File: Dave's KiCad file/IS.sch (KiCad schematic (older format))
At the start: 0 parts

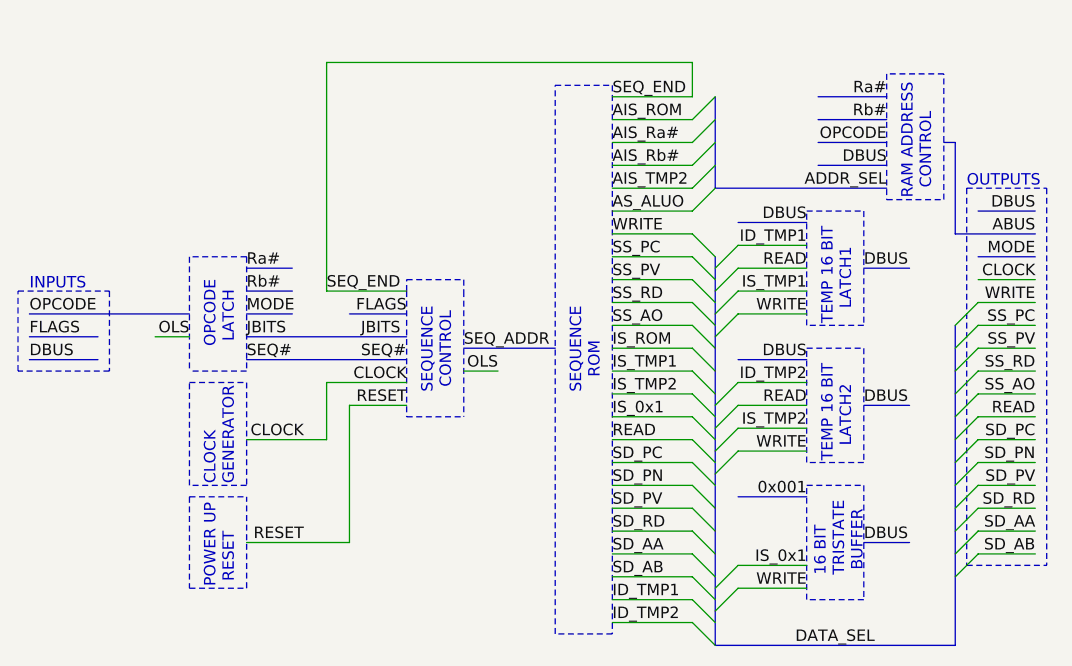
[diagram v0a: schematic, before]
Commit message: Add latch in RAM Address Control
Previously RET and POP Ra relied on using ALU output to put new SP value on RAM address, but that wouldn't work as can't have ALU output on data bus and use data bus for reading from RAM
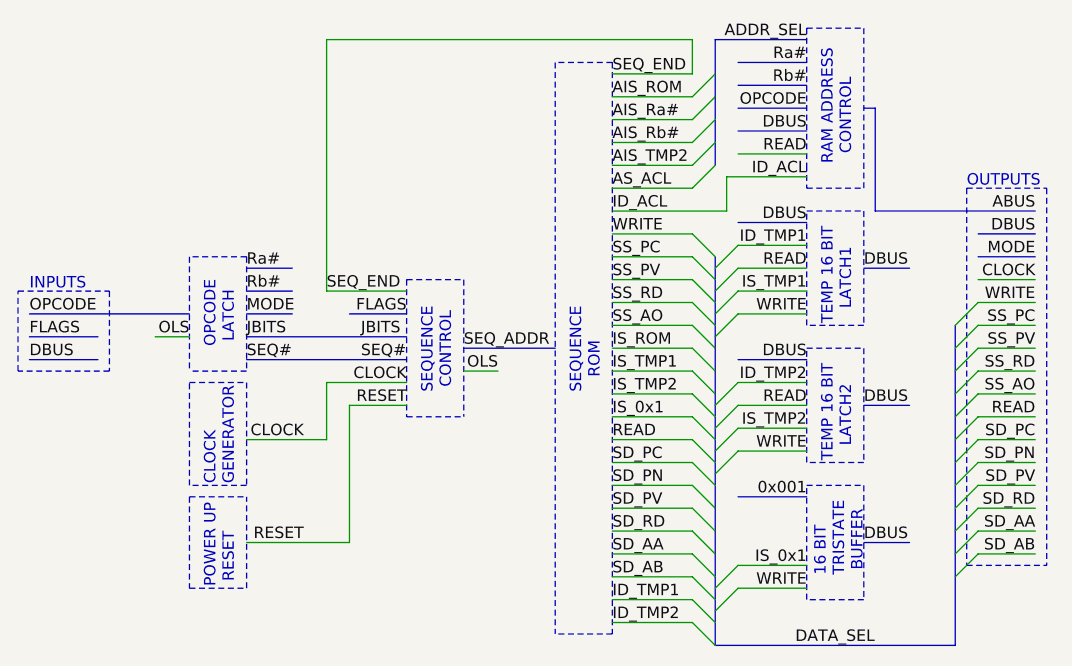
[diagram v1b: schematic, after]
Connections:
- net labels added: AS_ACL, ID_ACL
- net labels removed: AS_ALUO
- wire segments 59 -> 63
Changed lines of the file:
@@
 Text Label 3900 3750 0    50   ~ 0
 IS_0x1
+Text Label 3900 2350 0    50   ~ 0
+AIS_ROM
 Text Label 3900 2450 0    50   ~ 0
-AIS_ROM
+AIS_Ra#
 Text Label 3900 2550 0    50   ~ 0
-AIS_Ra#
+AIS_Rb#
 Text Label 3900 2650 0    50   ~ 0
-AIS_Rb#
+AIS_TMP2
 Text Label 3900 2750 0    50   ~ 0
-AIS_TMP2
-Text Label 3900 2850 0    50   ~ 0
-AS_ALUO
+AS_ACL
 Wire Wire Line
 	2050 3400 1900 3400
@@
 	2300 3550 2050 3550
 Wire Wire Line
+	3900 2650 4250 2650
+Wire Wire Line
+	3900 2550 4250 2550
+Wire Wire Line
+	3900 2450 4250 2450
+Wire Wire Line
+	3900 2350 4250 2350
+Wire Wire Line
 	3900 2750 4250 2750
-Wire Wire Line
-	3900 2650 4250 2650
-Wire Wire Line
-	3900 2550 4250 2550
-Wire Wire Line
-	3900 2450 4250 2450
-Wire Wire Line
-	3900 2850 4250 2850
 Wire Wire Line
 	3900 2950 4250 2950
@@
 	2300 3050 2050 3050
 Wire Wire Line
-	3900 2350 4250 2350
+	3900 2250 4250 2250
 Wire Notes Line style solid rgb(0, 255, 0)
 	2300 3050 2300 3550
 Wire Notes Line style solid rgb(0, 255, 0)
 	2050 3050 2050 3550
-Text Label 3900 2350 0    50   ~ 0
+Text Label 3900 2250 0    50   ~ 0
 SEQ_END
 Wire Notes Line style solid rgb(0, 255, 0)
-	3900 2300 3900 4700
-Wire Notes Line style solid rgb(0, 255, 0)
 	3900 4700 3650 4700
-Wire Notes Line style solid rgb(0, 255, 0)
-	3650 4700 3650 2300
-Wire Notes Line style solid rgb(0, 255, 0)
-	3650 2300 3900 2300
 Text Notes 3200 3650 1    50   ~ 0
 SEQUENCE\n CONTROL
@@
 	2300 3500 3000 3500
 Entry Wire Line
-	4250 2850 4350 2750
-Entry Wire Line
 	4250 2750 4350 2650
 Entry Wire Line
@@
 Entry Wire Line
 	4250 2450 4350 2350
-Text Notes 5300 2800 1    50   ~ 0
+Entry Wire Line
+	4250 2350 4350 2250
+Text Notes 4950 2650 1    50   ~ 0
 RAM ADDRESS\n  CONTROL
-Wire Bus Line
-	4350 2750 5100 2750
-Text Label 5100 2750 2    50   ~ 0
+Text Label 4750 2100 2    50   ~ 0
 ADDR_SEL
-Text Label 5100 2650 2    50   ~ 0
-DBUS
-Text Label 5100 2550 2    50   ~ 0
+Text Label 4750 2500 2    50   ~ 0
+DBUS
+Text Label 4750 2400 2    50   ~ 0
 OPCODE
 Wire Bus Line
-	5100 2550 4800 2550
-Text Label 5100 2350 2    50   ~ 0
+	4750 2400 4450 2400
+Text Label 4750 2200 2    50   ~ 0
 Ra#
-Text Label 5100 2450 2    50   ~ 0
+Text Label 4750 2300 2    50   ~ 0
 Rb#
 Wire Bus Line
-	4800 2650 5100 2650
-Wire Bus Line
-	4800 2450 5100 2450
-Wire Bus Line
-	4800 2350 5100 2350
-Wire Notes Line style solid rgb(0, 255, 0)
-	5100 2250 5100 2800
-Wire Notes Line style solid rgb(0, 255, 0)
-	5100 2800 5350 2800
-Wire Notes Line style solid rgb(0, 255, 0)
-	5350 2800 5350 2250
-Wire Notes Line style solid rgb(0, 255, 0)
-	5350 2250 5100 2250
+	4450 2300 4750 2300
+Wire Bus Line
+	4450 2200 4750 2200
 Wire Wire Line
 	3400 3550 3250 3550
@@
 Wire Bus Line
 	4450 2900 4750 2900
-Wire Notes Line style solid rgb(0, 255, 0)
-	3250 3200 3250 3750
-Wire Notes Line style solid rgb(0, 255, 0)
-	3000 3200 3000 3750
 Wire Bus Line
 	5000 3100 5200 3100
@@
 Wire Notes Line style solid rgb(0, 255, 0)
 	5000 3350 4750 3350
-Wire Bus Line
-	5400 2950 5750 2950
-Wire Bus Line
-	5400 2550 5350 2550
-Wire Bus Line
-	5400 2950 5400 2550
 Wire Notes Line
 	5800 2750 5800 4400
@@
 Wire Notes Line
 	5450 2750 5800 2750
+Text Label 5750 2950 2    50   ~ 0
+DBUS
+Wire Bus Line
+	5500 2950 5750 2950
 Text Label 5750 2850 2    50   ~ 0
-DBUS
-Wire Bus Line
-	5500 2850 5750 2850
-Text Label 5750 2950 2    50   ~ 0
 ABUS
 Entry Wire Line
@@
 	4750 4550 4750 4050
 Wire Wire Line
-	4250 2350 4250 2200
-Wire Wire Line
-	4250 2200 2650 2200
-Wire Wire Line
-	2650 2200 2650 3200
+	4250 2250 4250 2100
+Wire Wire Line
+	4250 2100 2650 2100
 Entry Wire Line
 	4350 4500 4450 4400
@@
 	2650 3200 3000 3200
 Wire Notes Line style solid rgb(0, 255, 0)
-	3000 3200 3000 3150
-Wire Notes Line style solid rgb(0, 255, 0)
 	3000 3150 3250 3150
 Wire Notes Line style solid rgb(0, 255, 0)
-	3250 3150 3250 3200
-Wire Bus Line
-	4350 2350 4350 2750
+	3250 3150 3250 3750
+Wire Notes Line style solid rgb(0, 255, 0)
+	3000 3150 3000 3750
+Text Label 4750 2600 2    50   ~ 0
+READ
+Wire Wire Line
+	4450 2600 4750 2600
+Text Label 3900 2850 0    50   ~ 0
+ID_ACL
+Wire Bus Line
+	4750 2500 4450 2500
+Wire Notes Line style solid rgb(0, 255, 0)
+	4750 2050 5000 2050
+Wire Notes Line style solid rgb(0, 255, 0)
+	4750 2050 4750 2650
+Wire Notes Line style solid rgb(0, 255, 0)
+	5000 2050 5000 2650
+Wire Bus Line
+	4350 2100 4750 2100
+Wire Bus Line
+	5050 2850 5750 2850
+Wire Wire Line
+	2650 2100 2650 3200
+Wire Notes Line style solid rgb(0, 255, 0)
+	3900 2200 3650 2200
+Wire Notes Line style solid rgb(0, 255, 0)
+	3900 2200 3900 4700
+Wire Notes Line style solid rgb(0, 255, 0)
+	3650 2200 3650 4700
+Wire Wire Line
+	3900 2850 4400 2850
+Wire Wire Line
+	4400 2700 4400 2850
+Wire Wire Line
+	4400 2700 4750 2700
+Text Label 4750 2700 2    50   ~ 0
+ID_ACL
+Wire Notes Line style solid rgb(0, 255, 0)
+	4750 2650 4750 2750
+Wire Notes Line style solid rgb(0, 255, 0)
+	4750 2750 5000 2750
+Wire Notes Line style solid rgb(0, 255, 0)
+	5000 2750 5000 2650
+Wire Bus Line
+	5000 2400 5050 2400
+Wire Bus Line
+	5050 2400 5050 2850
+Wire Bus Line
+	4350 2100 4350 2650
 Wire Bus Line
 	5400 3350 5400 4750

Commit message: Minor edits
Continuing work in progress on L1 IS design. Noticed some typos and minor improvements
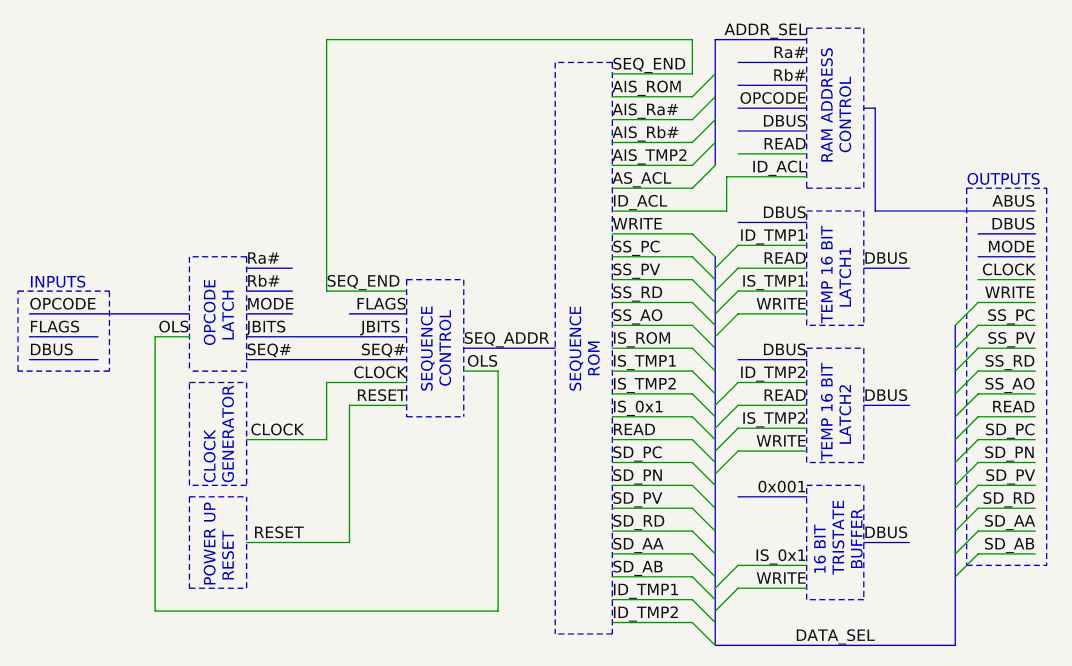
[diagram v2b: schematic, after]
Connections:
- wire segments 63 -> 66
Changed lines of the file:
@@
 Wire Notes Line style solid rgb(0, 255, 0)
 	4750 2050 5000 2050
-Wire Notes Line style solid rgb(0, 255, 0)
-	4750 2050 4750 2650
-Wire Notes Line style solid rgb(0, 255, 0)
-	5000 2050 5000 2650
 Wire Bus Line
 	4350 2100 4750 2100
@@
 ID_ACL
 Wire Notes Line style solid rgb(0, 255, 0)
-	4750 2650 4750 2750
-Wire Notes Line style solid rgb(0, 255, 0)
 	4750 2750 5000 2750
-Wire Notes Line style solid rgb(0, 255, 0)
-	5000 2750 5000 2650
 Wire Bus Line
 	5000 2400 5050 2400
 Wire Bus Line
 	5050 2400 5050 2850
+Wire Notes Line style solid rgb(0, 255, 0)
+	4750 2050 4750 2750
+Wire Notes Line style solid rgb(0, 255, 0)
+	5000 2050 5000 2750
+Wire Wire Line
+	3400 3550 3400 4600
+Wire Wire Line
+	3400 4600 1900 4600
+Wire Wire Line
+	1900 4600 1900 3400
 Wire Bus Line
 	4350 2100 4350 2650
